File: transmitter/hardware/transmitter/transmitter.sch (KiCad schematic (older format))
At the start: 14 parts

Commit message: Sensors
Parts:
- added J2: Conn_01x05, symbol Connector_Generic:Conn_01x05
- added R5: 10K, symbol Device:R
- added SW2: SW_SPST, symbol Switch:SW_SPST
- added TH1: Thermistor, symbol Device:Thermistor
- gave numbers to parts that had none: 14
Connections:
- net 3V3: now also SW2.1 (A)
- net GND: now also TH1.2
- net SENSE_PWR: now also R5.1
- net USB_UART_PWR: now reaches U1.15 (VIN)
- net USB_UART_PWR: now also SW2.2 (B)
- net at U3.1 (X4): now also J2.2 (Pin_2)
- net at U3.12 (X3): now also J2.1 (Pin_1)
- net TEMP_SENSE: now reaches U3.15 (X2)
- net TEMP_SENSE: now also R5.2, TH1.1
- net at U3.2 (X6): now also J2.4 (Pin_4)
- net at U3.4 (X7): now also J2.5 (Pin_5)
- net at U3.5 (X5): now also J2.3 (Pin_3)
- no-connect marks 21 -> 20
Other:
- note added: "Connect the power pin \nof the USB to UART chip,\nwith a bodge wire, to the VIN pin \nof the voltage regulator pad"
- note added: "Power"
- note added: "Sensors"
- moved on the sheet: BT1, C1, C2, C3, C4, SW1, U1, U2, U3

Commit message: Initial PCB layaout
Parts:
- BT1, J1, SW1, SW2, TH1: footprint (none) -> Connector_PinHeader_2.54mm:PinHeader_1x02_P2.54mm_Vertical
- C1, C2, C3, C4: footprint (none) -> Capacitor_SMD:C_0603_1608Metric_Pad1.05x0.95mm_HandSolder
- J2: footprint (none) -> Connector_PinHeader_2.54mm:PinHeader_1x05_P2.54mm_Vertical
- R1, R2, R3, R4, R5: footprint (none) -> Resistor_SMD:R_0603_1608Metric_Pad1.05x0.95mm_HandSolder
- U1: footprint (none) -> ESP8266:NodeMCU1.0(12-E)
- U3: footprint (none) -> Package_DIP:DIP-16_W7.62mm
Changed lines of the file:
@@
 EESchema Schematic File Version 4
+LIBS:transmitter-cache
 EELAYER 26 0
 EELAYER END
@@
 F 0 "U1" H 4300 4412 60  0000 C CNN
 F 1 "NodeMCU_1.0_(ESP-12E)" H 4300 4306 60  0000 C CNN
-F 2 "" H 3700 2475 60  0000 C CNN
+F 2 "ESP8266:NodeMCU1.0(12-E)" H 3700 2475 60  0001 C CNN
 F 3 "" H 3700 2475 60  0000 C CNN
 	1    4300 3325
@@
 F 0 "U3" H 6475 4575 50  0000 C CNN
 F 1 "CD4051B" H 6600 4500 50  0000 C CNN
-F 2 "" H 7000 3075 50  0001 L CNN
+F 2 "Package_DIP:DIP-16_W7.62mm" H 7000 3075 50  0001 L CNN
 F 3 "http://www.ti.com/lit/ds/symlink/cd4052b.pdf" H 6830 3925 50  0001 C CNN
 	1    6850 3825
@@
 F 0 "BT1" H 983 1421 50  0000 L CNN
 F 1 "Battery" H 983 1330 50  0000 L CNN
-F 2 "" V 875 1435 50  0001 C CNN
+F 2 "Connector_PinHeader_2.54mm:PinHeader_1x02_P2.54mm_Vertical" V 875 1435 50  0001 C CNN
 F 3 "~" V 875 1435 50  0001 C CNN
 	1    875  1375
@@
 F 0 "C3" H 1567 1421 50  0000 L CNN
 F 1 "1uF" H 1567 1330 50  0000 L CNN
-F 2 "" H 1475 1375 50  0001 C CNN
+F 2 "Capacitor_SMD:C_0603_1608Metric_Pad1.05x0.95mm_HandSolder" H 1475 1375 50  0001 C CNN
 F 3 "~" H 1475 1375 50  0001 C CNN
 	1    1475 1375
@@
 F 0 "C4" H 3042 1421 50  0000 L CNN
 F 1 "1uF" H 3042 1330 50  0000 L CNN
-F 2 "" H 2950 1375 50  0001 C CNN
+F 2 "Capacitor_SMD:C_0603_1608Metric_Pad1.05x0.95mm_HandSolder" H 2950 1375 50  0001 C CNN
 F 3 "~" H 2950 1375 50  0001 C CNN
 	1    2950 1375
@@
 F 0 "SW1" V 5054 2523 50  0000 L CNN
 F 1 "SW_SPST" V 5145 2523 50  0000 L CNN
-F 2 "" H 5100 2425 50  0001 C CNN
+F 2 "Connector_PinHeader_2.54mm:PinHeader_1x02_P2.54mm_Vertical" H 5100 2425 50  0001 C CNN
 F 3 "" H 5100 2425 50  0001 C CNN
 	1    5100 2425
@@
 F 0 "C1" H 6450 2650 50  0000 L CNN
 F 1 "0.1uf" H 6450 2550 50  0000 L CNN
-F 2 "" H 6725 2600 50  0001 C CNN
+F 2 "Capacitor_SMD:C_0603_1608Metric_Pad1.05x0.95mm_HandSolder" H 6725 2600 50  0001 C CNN
 F 3 "~" H 6725 2600 50  0001 C CNN
 	1    6725 2600
@@
 F 0 "C2" H 7217 2646 50  0000 L CNN
 F 1 "1uF" H 7217 2555 50  0000 L CNN
-F 2 "" H 7125 2600 50  0001 C CNN
+F 2 "Capacitor_SMD:C_0603_1608Metric_Pad1.05x0.95mm_HandSolder" H 7125 2600 50  0001 C CNN
 F 3 "~" H 7125 2600 50  0001 C CNN
 	1    7125 2600
@@
 F 0 "R1" H 10195 1296 50  0000 L CNN
 F 1 "100K" H 10195 1205 50  0000 L CNN
-F 2 "" V 10055 1250 50  0001 C CNN
+F 2 "Resistor_SMD:R_0603_1608Metric_Pad1.05x0.95mm_HandSolder" V 10055 1250 50  0001 C CNN
 F 3 "~" H 10125 1250 50  0001 C CNN
 	1    10125 1250
@@
 F 0 "R2" H 10195 1596 50  0000 L CNN
 F 1 "100K" H 10195 1505 50  0000 L CNN
-F 2 "" V 10055 1550 50  0001 C CNN
+F 2 "Resistor_SMD:R_0603_1608Metric_Pad1.05x0.95mm_HandSolder" V 10055 1550 50  0001 C CNN
 F 3 "~" H 10125 1550 50  0001 C CNN
 	1    10125 1550
@@
 F 0 "R3" H 10195 2796 50  0000 L CNN
 F 1 "10K" H 10195 2705 50  0000 L CNN
-F 2 "" V 10055 2750 50  0001 C CNN
+F 2 "Resistor_SMD:R_0603_1608Metric_Pad1.05x0.95mm_HandSolder" V 10055 2750 50  0001 C CNN
 F 3 "~" H 10125 2750 50  0001 C CNN
 	1    10125 2750
@@
 F 0 "J1" H 10454 2992 50  0000 L CNN
 F 1 "SOIL" H 10454 2901 50  0000 L CNN
-F 2 "" H 10375 3000 50  0001 C CNN
+F 2 "Connector_PinHeader_2.54mm:PinHeader_1x02_P2.54mm_Vertical" H 10375 3000 50  0001 C CNN
 F 3 "~" H 10375 3000 50  0001 C CNN
 	1    10375 3000
@@
 F 0 "R4" H 10195 3421 50  0000 L CNN
 F 1 "1K" H 10195 3330 50  0000 L CNN
-F 2 "" V 10055 3375 50  0001 C CNN
+F 2 "Resistor_SMD:R_0603_1608Metric_Pad1.05x0.95mm_HandSolder" V 10055 3375 50  0001 C CNN
 F 3 "~" H 10125 3375 50  0001 C CNN
 	1    10125 3375
@@
 Data
 89 50 4E 47 0D 0A 1A 0A 00 00 00 0D 49 48 44 52 00 00 02 FC 00 00 01 FD 08 02 00 00 00 E9 8E 3F
-E0 00 00 00 03 73 42 49 54 08 08 08 DB E1 4F E0 00 00 00 09 70 48 59 73 00 00 0B 12 00 00 0B 12
-01 D2 DD 7E FC 00 00 20 00 49 44 41 54 78 9C 44 BB D7 CE 64 4B 76 26 B6 4C 98 6D D2 E7 EF AA 4E
+E0 00 00 00 03 73 42 49 54 08 08 08 DB E1 4F E0 00 00 00 09 70 48 59 73 00 00 0A F0 00 00 0A F0
+01 42 AC 34 98 00 00 20 00 49 44 41 54 78 9C 44 BB D7 CE 64 4B 76 26 B6 4C 98 6D D2 E7 EF AA 4E
 D5 A9 53 ED 5B AD 1E 6A 44 91 A3 11 45 0C 34 D7 82 9E 4B 10 A0 77 19 40 CF 20 8A 23 42 33 60 CF
 B0 0D D9 A7 8F 29 FF DB B4 DB 44 C4 5A 4B 17 BB 0E 19 48 24 F2 22 33 11 7B EF 88 B5 3E 17 F8 7F
@@
 F 0 "R5" H 10245 4446 50  0000 L CNN
 F 1 "10K" H 10245 4355 50  0000 L CNN
-F 2 "" V 10105 4400 50  0001 C CNN
+F 2 "Resistor_SMD:R_0603_1608Metric_Pad1.05x0.95mm_HandSolder" V 10105 4400 50  0001 C CNN
 F 3 "~" H 10175 4400 50  0001 C CNN
 	1    10175 4400
@@
 F 0 "TH1" H 10280 4896 50  0000 L CNN
 F 1 "Thermistor" H 10280 4805 50  0000 L CNN
-F 2 "" H 10175 4850 50  0001 C CNN
+F 2 "Connector_PinHeader_2.54mm:PinHeader_1x02_P2.54mm_Vertical" H 10175 4850 50  0001 C CNN
 F 3 "~" H 10175 4850 50  0001 C CNN
 	1    10175 4850
@@
 F 0 "J2" H 8075 4425 50  0000 L CNN
 F 1 "Conn_01x05" H 7925 3825 50  0000 L CNN
-F 2 "" H 8125 4125 50  0001 C CNN
+F 2 "Connector_PinHeader_2.54mm:PinHeader_1x05_P2.54mm_Vertical" H 8125 4125 50  0001 C CNN
 F 3 "~" H 8125 4125 50  0001 C CNN
 	1    8125 4125
@@
 F 0 "SW2" H 2500 4610 50  0000 C CNN
 F 1 "SW_SPST" H 2500 4519 50  0000 C CNN
-F 2 "" H 2500 4375 50  0001 C CNN
+F 2 "Connector_PinHeader_2.54mm:PinHeader_1x02_P2.54mm_Vertical" H 2500 4375 50  0001 C CNN
 F 3 "" H 2500 4375 50  0001 C CNN
 	1    2500 4375

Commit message: Layout
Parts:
- removed J2: Conn_01x05, Connector_PinHeader_2.54mm:PinHeader_1x05_P2.54mm_Vertical, symbol Connector_Generic:Conn_01x05
- removed SW2: SW_SPST, Connector_PinHeader_2.54mm:PinHeader_1x02_P2.54mm_Vertical, symbol Switch:SW_SPST
- added J3: USB_UART_OFF, Connector_PinHeader_2.54mm:PinHeader_1x01_P2.54mm_Vertical, symbol Connector_Generic:Conn_01x01
- added J4: USB_UART_ON, Connector_PinHeader_2.54mm:PinHeader_1x01_P2.54mm_Vertical, symbol Connector_Generic:Conn_01x01
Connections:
- net 3V3: now also J4.1 (Pin_1)
- net GND: now also J3.1 (Pin_1)
- net USB_UART_PWR: no longer names the net of U1.15 (VIN)
- no-connect marks 20 -> 26
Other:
- note added: "Connect the power pin \nof the USB to UART chip,\nwith a bodge wire, \nto either off or on."
- note removed: "Connect the power pin \nof the USB to UART chip,\nwith a bodge wire, to the VIN pin \nof the voltage regulator pad"
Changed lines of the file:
@@
 Text GLabel 7350 3825 2    50   Input ~ 0
 TEMP_SENSE
-$Comp
-L Connector_Generic:Conn_01x05 J2
-U 1 1 5DBD3F8C
-P 8125 4125
-F 0 "J2" H 8075 4425 50  0000 L CNN
-F 1 "Conn_01x05" H 7925 3825 50  0000 L CNN
-F 2 "Connector_PinHeader_2.54mm:PinHeader_1x05_P2.54mm_Vertical" H 8125 4125 50  0001 C CNN
-F 3 "~" H 8125 4125 50  0001 C CNN
-	1    8125 4125
-	1    0    0    -1
-$EndComp
-Wire Wire Line
-	7350 3925 7925 3925
-Wire Wire Line
-	7925 4025 7350 4025
-Wire Wire Line
-	7350 4125 7925 4125
-Wire Wire Line
-	7925 4225 7350 4225
-Wire Wire Line
-	7350 4325 7925 4325
-$Comp
-L Switch:SW_SPST SW2
-U 1 1 5DBD72AE
-P 2500 4375
-F 0 "SW2" H 2500 4610 50  0000 C CNN
-F 1 "SW_SPST" H 2500 4519 50  0000 C CNN
-F 2 "Connector_PinHeader_2.54mm:PinHeader_1x02_P2.54mm_Vertical" H 2500 4375 50  0001 C CNN
-F 3 "" H 2500 4375 50  0001 C CNN
-	1    2500 4375
-	1    0    0    -1
-$EndComp
-Text Notes 4150 6325 0    50   ~ 0
-Connect the power pin \nof the USB to UART chip,\nwith a bodge wire, to the VIN pin \nof the voltage regulator pad
-Wire Notes Line width 28 rgb(0, 194, 0)
-	3300 6175 2700 6175
-Wire Notes Line width 28 rgb(0, 194, 0)
-	2700 6175 2700 6350
+Text Notes 4350 6100 0    50   ~ 0
+Connect the power pin \nof the USB to UART chip,\nwith a bodge wire, \nto either off or on.
 Text GLabel 3525 1175 2    50   Input ~ 0
 3V3
@@
 Wire Wire Line
 	3100 3925 3100 3950
-Wire Wire Line
-	3500 4025 3500 4375
-Wire Wire Line
-	3500 4375 2700 4375
-Text GLabel 2300 4375 0    50   Input ~ 0
+Text GLabel 4750 5175 2    50   Input ~ 0
 3V3
-Text Label 2800 4375 0    50   ~ 0
-USB_UART_PWR
 Wire Notes Line
 	600  650  3775 650
@@
 Text Notes 9100 775  0    50   ~ 10
 Sensors
+NoConn ~ 3500 4025
+$Comp
+L Connector_Generic:Conn_01x01 J3
+U 1 1 5DBC844A
+P 4550 5550
+F 0 "J3" H 4550 5425 50  0000 C CNN
+F 1 "USB_UART_OFF" H 4500 5675 50  0000 C CNN
+F 2 "Connector_PinHeader_2.54mm:PinHeader_1x01_P2.54mm_Vertical" H 4550 5550 50  0001 C CNN
+F 3 "~" H 4550 5550 50  0001 C CNN
+	1    4550 5550
+	-1   0    0    1
+$EndComp
+Wire Notes Line width 31 rgb(0, 194, 0)
+	4275 6175 4275 5550
+Wire Notes Line width 31 rgb(0, 194, 0)
+	4275 5550 4525 5550
+Wire Notes Line width 31 rgb(0, 194, 0)
+	3300 6175 4275 6175
+$Comp
+L Connector_Generic:Conn_01x01 J4
+U 1 1 5DBCB146
+P 4550 5175
+F 0 "J4" H 4550 5050 50  0000 C CNN
+F 1 "USB_UART_ON" H 4525 5300 50  0000 C CNN
+F 2 "Connector_PinHeader_2.54mm:PinHeader_1x01_P2.54mm_Vertical" H 4550 5175 50  0001 C CNN
+F 3 "~" H 4550 5175 50  0001 C CNN
+	1    4550 5175
+	-1   0    0    1
+$EndComp
+$Comp
+L power:GND #PWR010
+U 1 1 5DBCB1FE
+P 5325 5550
+F 0 "#PWR010" H 5325 5300 50  0001 C CNN
+F 1 "GND" H 5330 5377 50  0000 C CNN
+F 2 "" H 5325 5550 50  0001 C CNN
+F 3 "" H 5325 5550 50  0001 C CNN
+	1    5325 5550
+	1    0    0    -1
+$EndComp
+Wire Wire Line
+	4750 5550 5325 5550
+NoConn ~ 7350 3925
+NoConn ~ 7350 4025
+NoConn ~ 7350 4125
+NoConn ~ 7350 4225
+NoConn ~ 7350 4325
 $EndSCHEMATC

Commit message: Power traces
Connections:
- net 3V3: now also U1.16 (3.3V), U1.25 (3.3V)
- net GND: now also U1.10 (GND), U1.17 (GND), U1.24 (GND)
- no-connect marks 26 -> 21
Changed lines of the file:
@@
 Text GLabel 3500 3825 0    50   Input ~ 0
 RESET
-NoConn ~ 3500 3525
 Text GLabel 5100 2050 0    50   Input ~ 0
 RESET
@@
 NoConn ~ 5100 2925
 NoConn ~ 5100 3025
-NoConn ~ 5100 3125
-NoConn ~ 5100 3225
 NoConn ~ 5100 3625
 NoConn ~ 5100 3725
 NoConn ~ 5100 3825
-NoConn ~ 5100 3925
-NoConn ~ 5100 4025
 $Comp
 L Device:R R1
@@
 NoConn ~ 7350 4225
 NoConn ~ 7350 4325
+$Comp
+L power:GND #PWR0101
+U 1 1 5DBCB76A
+P 5500 3925
+F 0 "#PWR0101" H 5500 3675 50  0001 C CNN
+F 1 "GND" H 5505 3752 50  0000 C CNN
+F 2 "" H 5500 3925 50  0001 C CNN
+F 3 "" H 5500 3925 50  0001 C CNN
+	1    5500 3925
+	1    0    0    -1
+$EndComp
+Text GLabel 5100 4025 2    50   Input ~ 0
+3V3
+Wire Wire Line
+	5100 3925 5500 3925
+$Comp
+L power:GND #PWR0102
+U 1 1 5DBCC291
+P 3100 3525
+F 0 "#PWR0102" H 3100 3275 50  0001 C CNN
+F 1 "GND" H 3105 3352 50  0000 C CNN
+F 2 "" H 3100 3525 50  0001 C CNN
+F 3 "" H 3100 3525 50  0001 C CNN
+	1    3100 3525
+	1    0    0    -1
+$EndComp
+Wire Wire Line
+	3500 3525 3100 3525
+$Comp
+L power:GND #PWR0103
+U 1 1 5DBCCC45
+P 5500 3225
+F 0 "#PWR0103" H 5500 2975 50  0001 C CNN
+F 1 "GND" H 5500 3275 50  0000 C CNN
+F 2 "" H 5500 3225 50  0001 C CNN
+F 3 "" H 5500 3225 50  0001 C CNN
+	1    5500 3225
+	1    0    0    -1
+$EndComp
+Wire Wire Line
+	5100 3225 5500 3225
+Text GLabel 5100 3125 2    50   Input ~ 0
+3V3
 $EndSCHEMATC

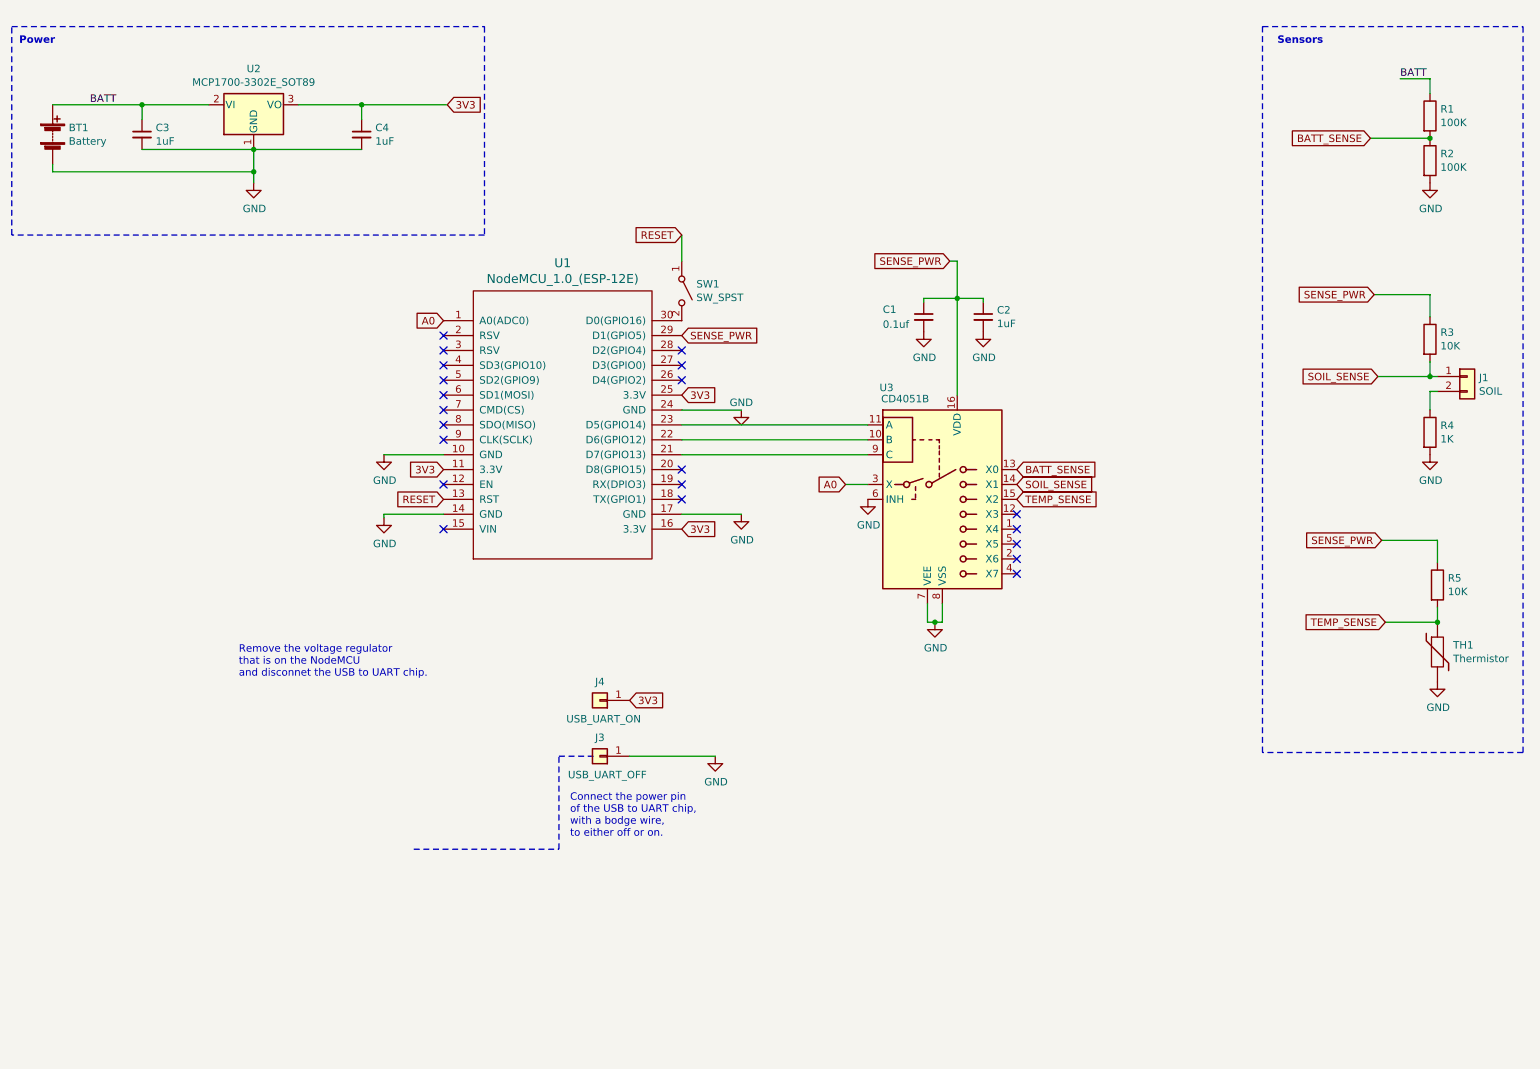
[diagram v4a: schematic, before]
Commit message: Multiple soil sensors
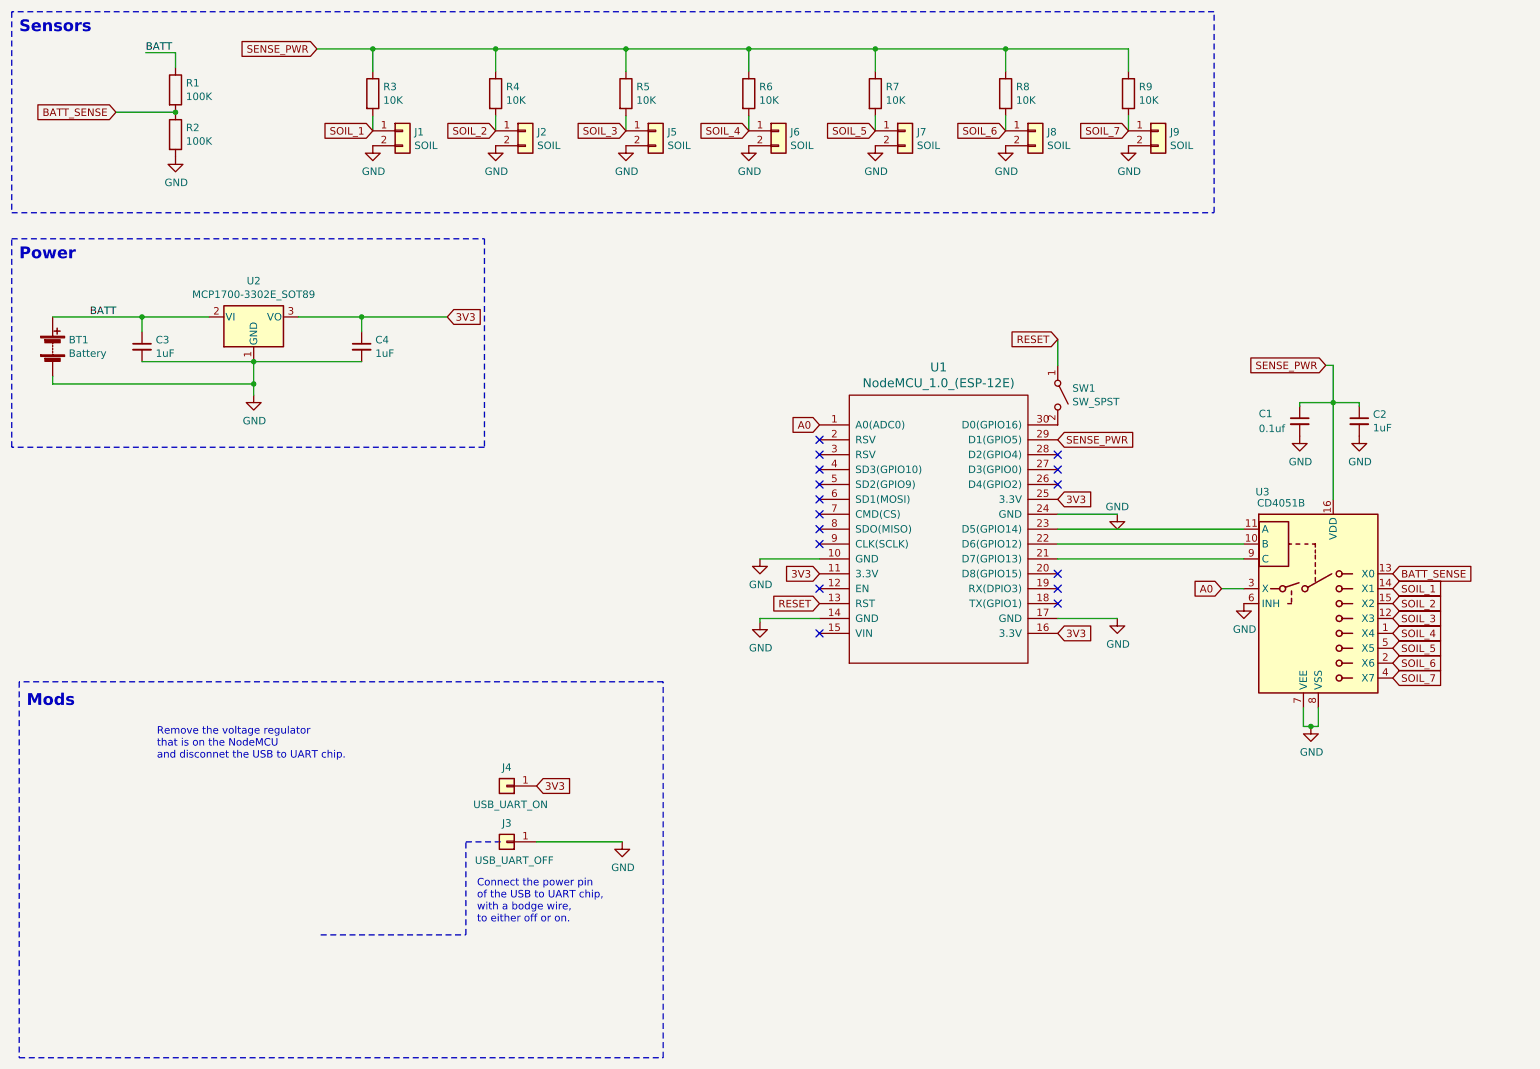
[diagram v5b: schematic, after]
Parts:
- removed TH1: Thermistor, Connector_PinHeader_2.54mm:PinHeader_1x02_P2.54mm_Vertical, symbol Device:Thermistor
- added J2, J5, J6, J7, J8, J9: SOIL, Connector_PinHeader_2.54mm:PinHeader_1x02_P2.54mm_Vertical, symbol Connector_Generic:Conn_01x02
- added R6, R7, R8, R9: 10K, Resistor_SMD:R_0603_1608Metric_Pad1.05x0.95mm_HandSolder, symbol Device:R
- R4: value 1K -> 10K
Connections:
- net GND: now also J1.2 (Pin_2), J2.2 (Pin_2), J5.2 (Pin_2), J6.2 (Pin_2), J7.2 (Pin_2), J8.2 (Pin_2), J9.2 (Pin_2); no longer R4.2
- net SENSE_PWR: now also R4.1, R6.1, R7.1, R8.1, R9.1
- net SOIL_4: now reaches U3.1 (X4)
- net SOIL_4: now also J6.1 (Pin_1), R6.2
- net SOIL_3: now reaches U3.12 (X3)
- net SOIL_3: now also R5.2, J5.1 (Pin_1)
- net SOIL_6: now reaches U3.2 (X6)
- net SOIL_6: now also J8.1 (Pin_1), R8.2
- net SOIL_7: now reaches U3.4 (X7)
- net SOIL_7: now also J9.1 (Pin_1), R9.2
- net SOIL_5: now reaches U3.5 (X5)
- net SOIL_5: now also J7.1 (Pin_1), R7.2
- net SOIL_SENSE renamed SOIL_1
- net TEMP_SENSE renamed SOIL_2
- net SOIL_2: now also R4.2, J2.1 (Pin_1); no longer R5.2
- no-connect marks 21 -> 16
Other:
- note added: "Mods"
- moved on the sheet: BT1, C1, C2, C3, C4, J1, J3, J4, R1, R2, R3, SW1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
